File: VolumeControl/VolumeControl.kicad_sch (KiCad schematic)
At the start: 10 parts, among them J1 Barrel_Jack, U1 OPA1612AxD, U2 MCP4251-xxxx-SL, U3 L7812

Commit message: adv1
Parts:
- added C4: C, symbol Device:C
- added R2: R, symbol Device:R
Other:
- moved on the sheet: R1

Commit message: 6 Opamps
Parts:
- removed D1: 1N4001, Diode_THT:D_DO-41_SOD81_P10.16mm_Horizontal, symbol Diode:1N4001
- added C10, C11, C14, C15, C16, C17, C20, C21, C7, C8, C9: 10u, symbol Device:C
- added C12, C13, C18, C19, C5, C6: 50p, symbol Device:C
- added J10, J11, J12, J13, J2, J3, J4, J5, J6, J7, J8, J9: Conn_01x03, symbol Connector_Generic:Conn_01x03
- added R10, R11, R12, R3, R4, R5, R6, R7, R8, R9: 100k, Resistor_SMD:R_0805_2012Metric, symbol Device:R
- added U4, U6: MCP4251-xxxx-SL, Package_SO:SOIC-14_3.9x8.7mm_P1.27mm, symbol Potentiometer_Digital:MCP4251-xxxx-SL
- added U5, U7: OPA1612AxD, symbol Amplifier_Operational:OPA1612AxD
- C4: value C -> 10u
- R2: value R -> 100k; footprint (none) -> Resistor_SMD:R_0805_2012Metric
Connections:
- net GND: now also C1.2, C2.2, C3.2, J1.2, R1.2, R2.2, U1.4 (V-), U2.4 (VSS), C12.1, C13.1, C18.1, C19.1, C5.1, C6.1, J10.1 (Pin_1), J11.1 (Pin_1), J12.1 (Pin_1), J13.1 (Pin_1), J2.1 (Pin_1), J3.1 (Pin_1), J4.1 (Pin_1), J5.1 (Pin_1), J6.1 (Pin_1), J7.1 (Pin_1), J8.1 (Pin_1), J9.1 (Pin_1), R10.2, R11.2, R12.2, R3.2, R4.2, R5.2, R6.2, R7.2, R8.2, R9.2, U4.4 (VSS), U6.4 (VSS)
- net REF: now also U4.10 (P0B), U4.5 (P1B), U6.10 (P0B), U6.5 (P1B)
- net at R1.1: now also C4.2, J3.2 (Pin_2)
- net at C4.1: now also U1.1, U1.2 (-), C5.2
- net at U1.6 (-), U1.7: now also C6.2, C7.1
- net VCC: now reaches C1.1
- net VCC: now also C2.1, U1.8 (V+), U2.14 (VDD), U3.3 (OUT), U4.14 (VDD), U6.14 (VDD)
- net at R2.1: now also C7.2, J4.2 (Pin_2)
- net at C3.1: now also D2.1 (K), U3.1 (IN)
- net at U2.7 (P1A): now also C8.2
- net at U2.8 (P0A): now also C9.2
- net at D2.2 (A): now also J1.1
- new net: C18.2, C20.1, U7.1, U7.2 (-)
- new net: C20.2, J12.2 (Pin_2), R11.1
- new net: U4.6 (P1W), U5.5 (+)
- new net: C10.2, U4.7 (P1A)
- new net: C11.2, U4.8 (P0A)
- new net: U4.9 (P0W), U5.3 (+)
- new net: C9.1, J5.2 (Pin_2), R4.1
- new net: C19.2, C21.1, U7.6 (-), U7.7
- new net: C21.2, J13.2 (Pin_2), R12.1
- new net: C12.2, C14.1, U5.1, U5.2 (-)
- new net: C17.1, J11.2 (Pin_2), R10.1
- new net: C8.1, J2.2 (Pin_2), R3.1
- new net: C16.1, J10.2 (Pin_2), R9.1
- new net: U6.6 (P1W), U7.5 (+)
- new net: C16.2, U6.7 (P1A)
- new net: C17.2, U6.8 (P0A)
- new net: U6.9 (P0W), U7.3 (+)
- new net: C13.2, C15.1, U5.6 (-), U5.7
- new net: C15.2, J9.2 (Pin_2), R8.1
- new net: C10.1, J6.2 (Pin_2), R5.1
- new net: C14.2, J8.2 (Pin_2), R7.1
- new net: C11.1, J7.2 (Pin_2), R6.1
- new net Earth: J10.3 (Pin_3), J11.3 (Pin_3), J12.3 (Pin_3), J13.3 (Pin_3), J2.3 (Pin_3), J3.3 (Pin_3), J4.3 (Pin_3), J5.3 (Pin_3), J6.3 (Pin_3), J7.3 (Pin_3), J8.3 (Pin_3), J9.3 (Pin_3)
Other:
- moved on the sheet: C1, C2, C3, C4, D2, J1, R1, U1A, U1B, U1C, U2, U3

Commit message: circuito quase completo
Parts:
- added C22, C23: 50p, Capacitor_SMD:C_0805_2012Metric_Pad1.18x1.45mm_HandSolder, symbol Device:C
- added C24, C25, C26, C27, C28: 100nF, Capacitor_SMD:C_0805_2012Metric, symbol Device:C
- added C29: 100uF, Capacitor_SMD:CP_Elec_5x3.9, symbol Device:C_Polarized
- added R13, R14, R15: 100k, Resistor_SMD:R_0805_2012Metric, symbol Device:R
- added U10: LM1117MP-5.0, Package_TO_SOT_SMD:SOT-223-3_TabPin2, symbol Regulator_Linear:LM1117MP-5.0
- added U8: OPA1612AxD, Package_SO:SOIC-8-1EP_3.9x4.9mm_P1.27mm_EP2.29x3mm, symbol Amplifier_Operational:OPA1612AxD
- added U9: WEMOS_D1_mini, RF_Module:WEMOS_D1_mini_light, symbol RF_Module:WEMOS_D1_mini
- C1: footprint Capacitor_SMD:C_0805_2012Metric -> Capacitor_SMD:C_0805_2012Metric_Pad1.18x1.45mm_HandSolder
- C10, C11, C14, C15, C16, C17, C20, C21, C4, C7, C8, C9: footprint (none) -> Capacitor_SMD:C_1210_3225Metric_Pad1.33x2.70mm_HandSolder
- C12, C13, C18, C19, C5, C6: footprint (none) -> Capacitor_SMD:C_0805_2012Metric_Pad1.18x1.45mm_HandSolder
- C2, C3: value C_Polarized -> 100uF; footprint (none) -> Capacitor_SMD:CP_Elec_5x3.9
- J1: footprint (none) -> Connector_BarrelJack:BarrelJack_CUI_PJ-063AH_Horizontal
- J10, J11, J12, J13, J2, J3, J4, J5, J6, J7, J8, J9: footprint (none) -> Connector_PinHeader_1.00mm:PinHeader_1x03_P1.00mm_Vertical
- U1, U5, U7: footprint (none) -> Package_SO:SOIC-8-1EP_3.9x4.9mm_P1.27mm_EP2.29x3mm
- U3: footprint (none) -> Package_TO_SOT_SMD:TO-252-3_TabPin2
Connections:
- net GND: now also U5.4 (V-), U7.4 (V-), C22.1, C23.1, C24.2, C25.2, C26.2, C27.2, C28.2, C29.2, R13.2, R15.2, U10.1 (GND), U8.4 (V-), U9.10 (GND)
- net REF: now also C23.2, U8.1, U8.2 (-)
- net VCC: now also U5.8 (V+), U7.8 (V+), C24.1, C25.1, C26.1, C27.1, R14.1, U10.3 (VI), U8.8 (V+)
- new net: R15.1, U8.7
- new net: C22.2, R13.1, R14.2, U8.3 (+)
- new net V5V: C28.1, C29.1, U10.2 (VO), U9.9 (5V)
- no-connect marks 0 -> 2
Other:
- moved on the sheet: C1, C2, C3, D2, J1, U1C, U3

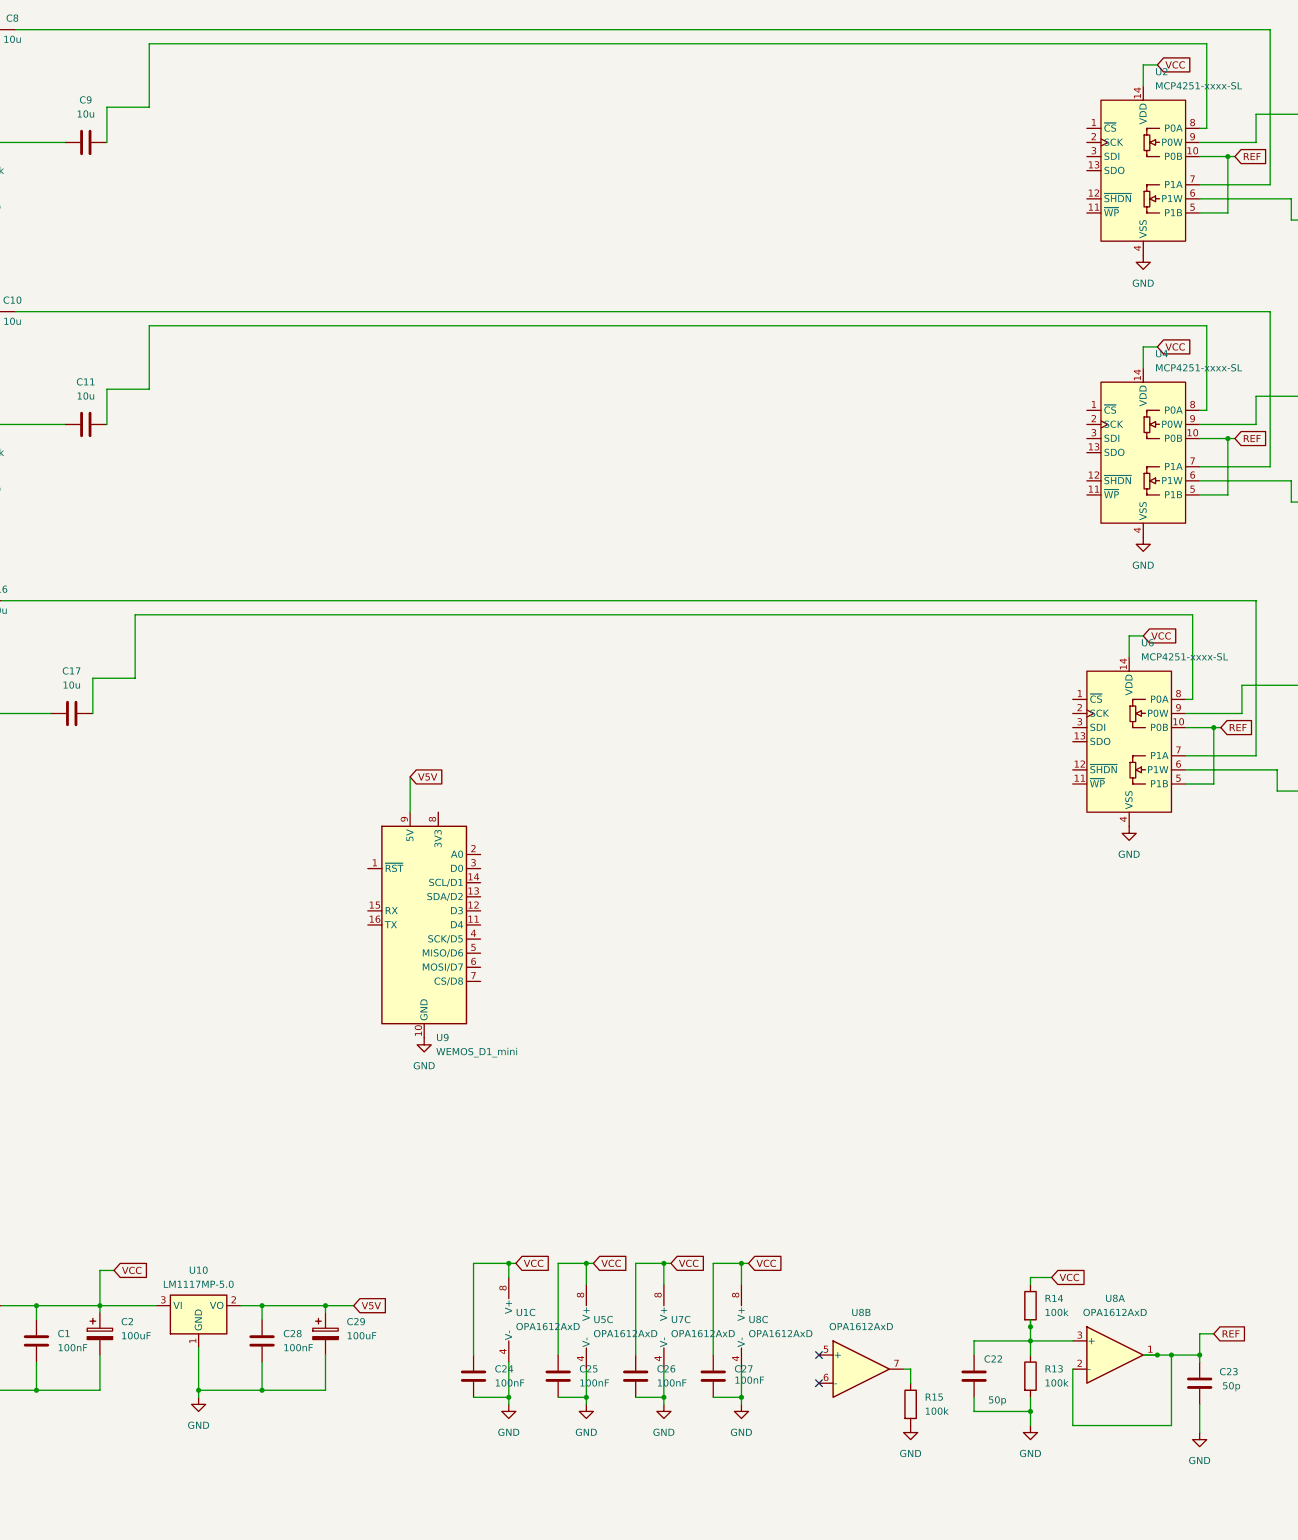
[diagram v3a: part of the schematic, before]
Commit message: changing power supply of dig potentiometers
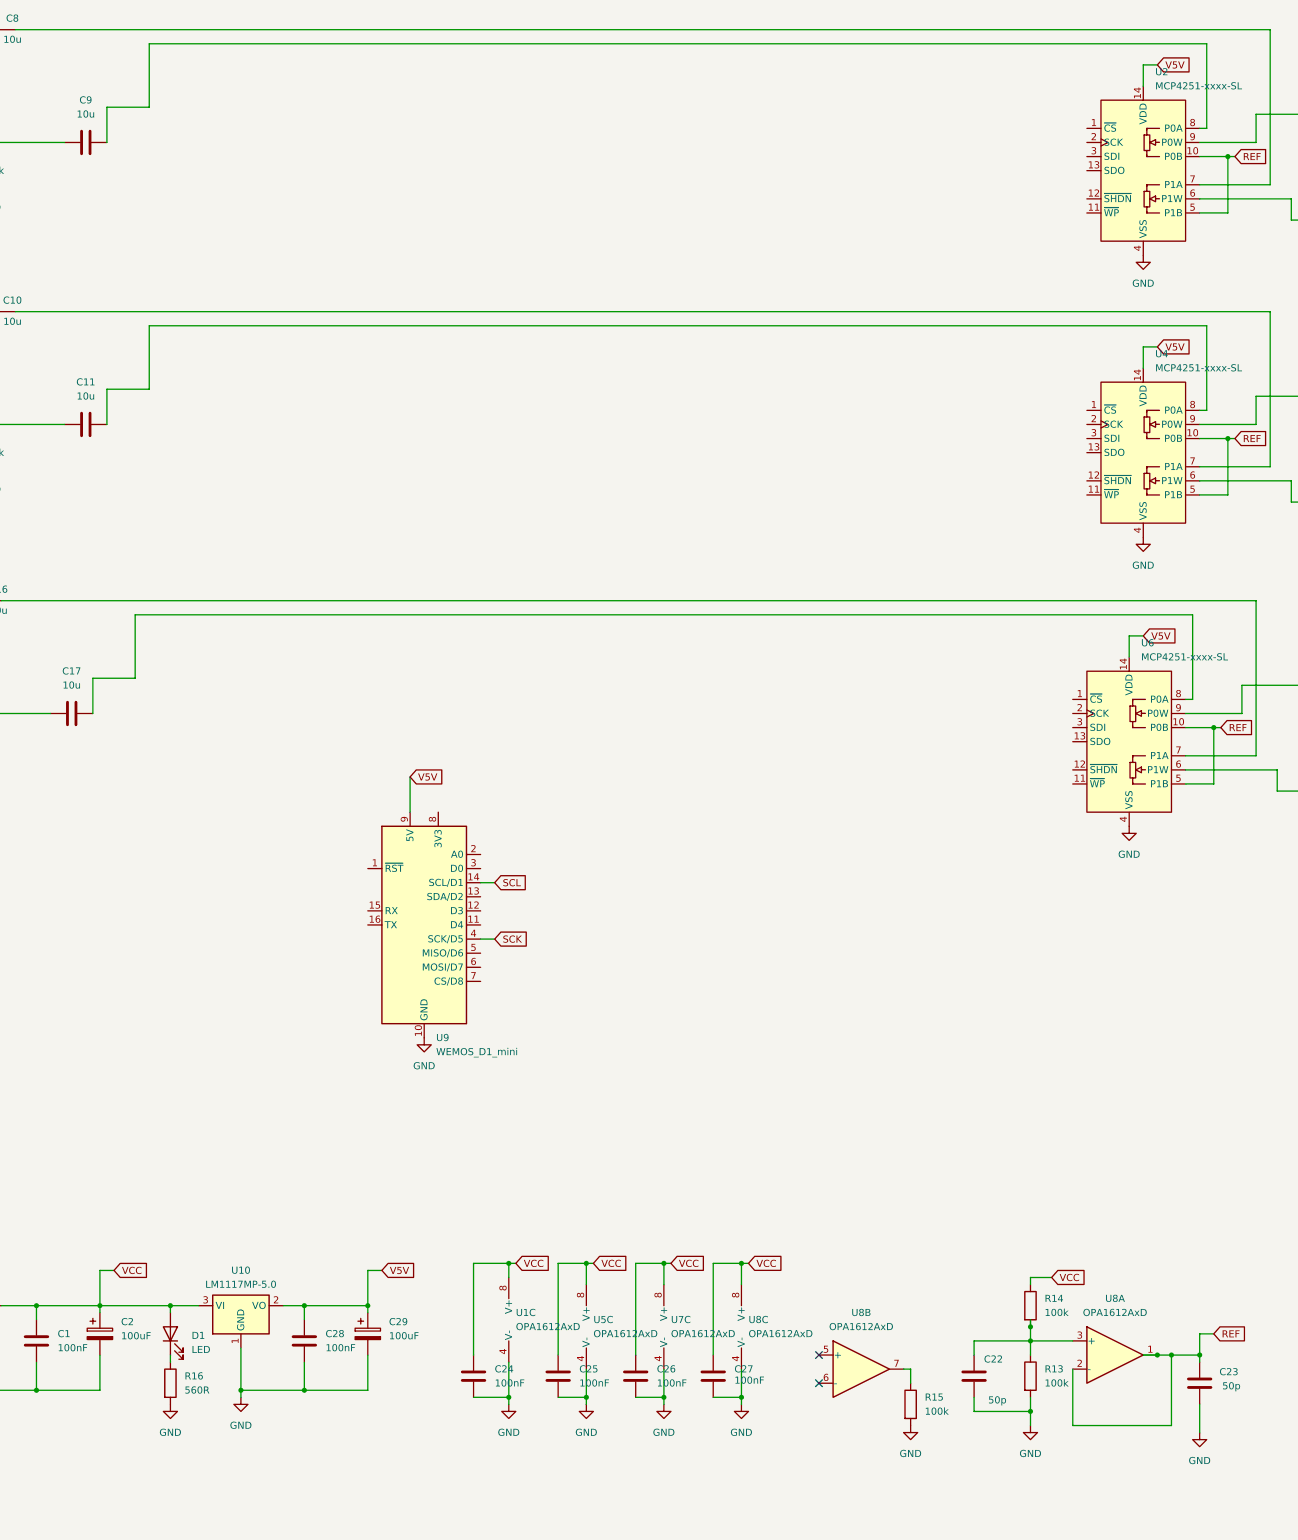
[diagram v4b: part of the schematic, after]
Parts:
- added D1: LED, symbol Device:LED
- added R16: 560R, Resistor_SMD:R_0805_2012Metric, symbol Device:R
- added unit 3 of U5
- added unit 3 of U7
- added unit 2 of U8
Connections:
- net GND: now also R16.2, U5.4 (V-), U7.4 (V-); no longer U5.4 (V-), U7.4 (V-)
- net V5V: now also U2.14 (VDD), U4.14 (VDD), U6.14 (VDD)
- net VCC: now also D1.2 (A), U5.8 (V+), U7.8 (V+); no longer U2.14 (VDD), U4.14 (VDD), U5.8 (V+), U6.14 (VDD), U7.8 (V+)
- net SCL: now reaches U9.14 (SCL/D1)
- net SCK: now reaches U9.4 (SCK/D5)
- net at R15.1: now also U8.7; no longer U8.7
- new net: D1.1 (K), R16.1
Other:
- moved on the sheet: C28, C29, U10

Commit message: layout upates
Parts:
- D1: footprint (none) -> LED_SMD:LED_1210_3225Metric
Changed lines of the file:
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@@
 			)
 		)
-		(property "Footprint" ""
+		(property "Footprint" "LED_SMD:LED_1210_3225Metric"
 			(at 104.14 255.27 0)
 			(effects

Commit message: improvements on PCB design - PCB placement finished -missing controller
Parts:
- added FB1: FerriteBead_Small, Resistor_SMD:R_1206_3216Metric_Pad1.30x1.75mm_HandSolder, symbol Device:FerriteBead_Small
- added R17: 10R, Resistor_SMD:R_0805_2012Metric, symbol Device:R
- U1, U5, U7, U8: footprint Package_SO:SOIC-8-1EP_3.9x4.9mm_P1.27mm_EP2.29x3mm -> Package_SO:SOIC-8_3.9x4.9mm_P1.27mm
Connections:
- net Earth: now also FB1.1, R17.1
- net GND: now also FB1.2, R17.2

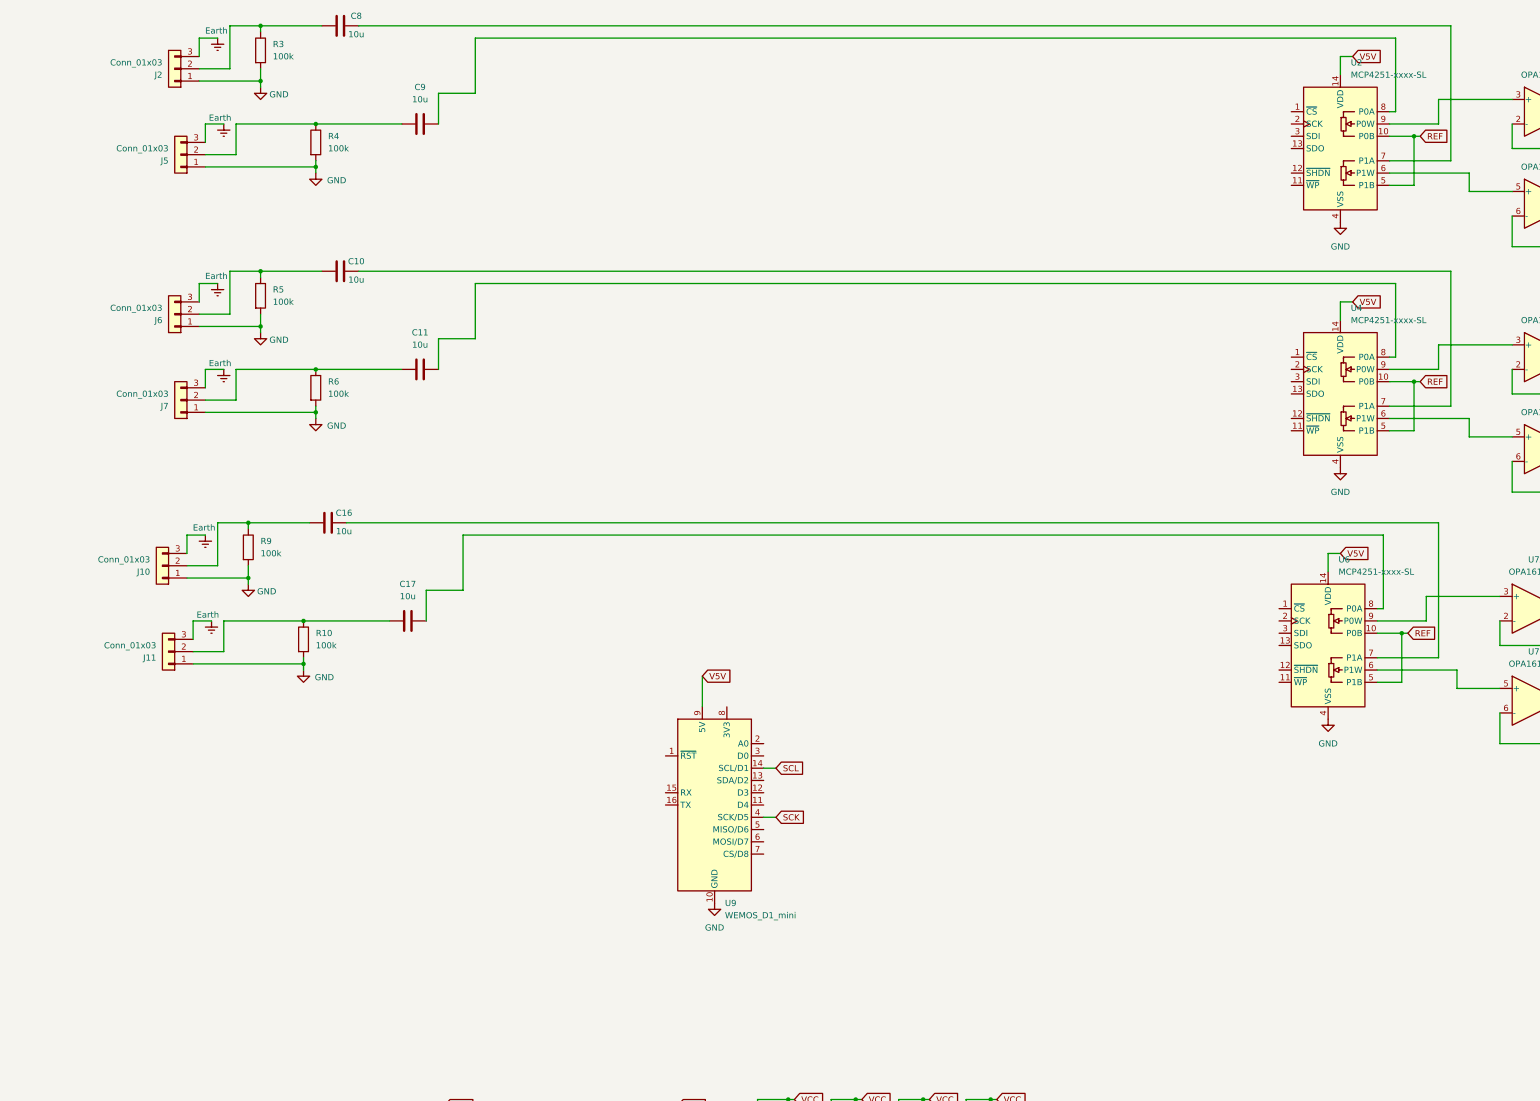
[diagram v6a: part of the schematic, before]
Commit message: simulation update, schematic update for only one input
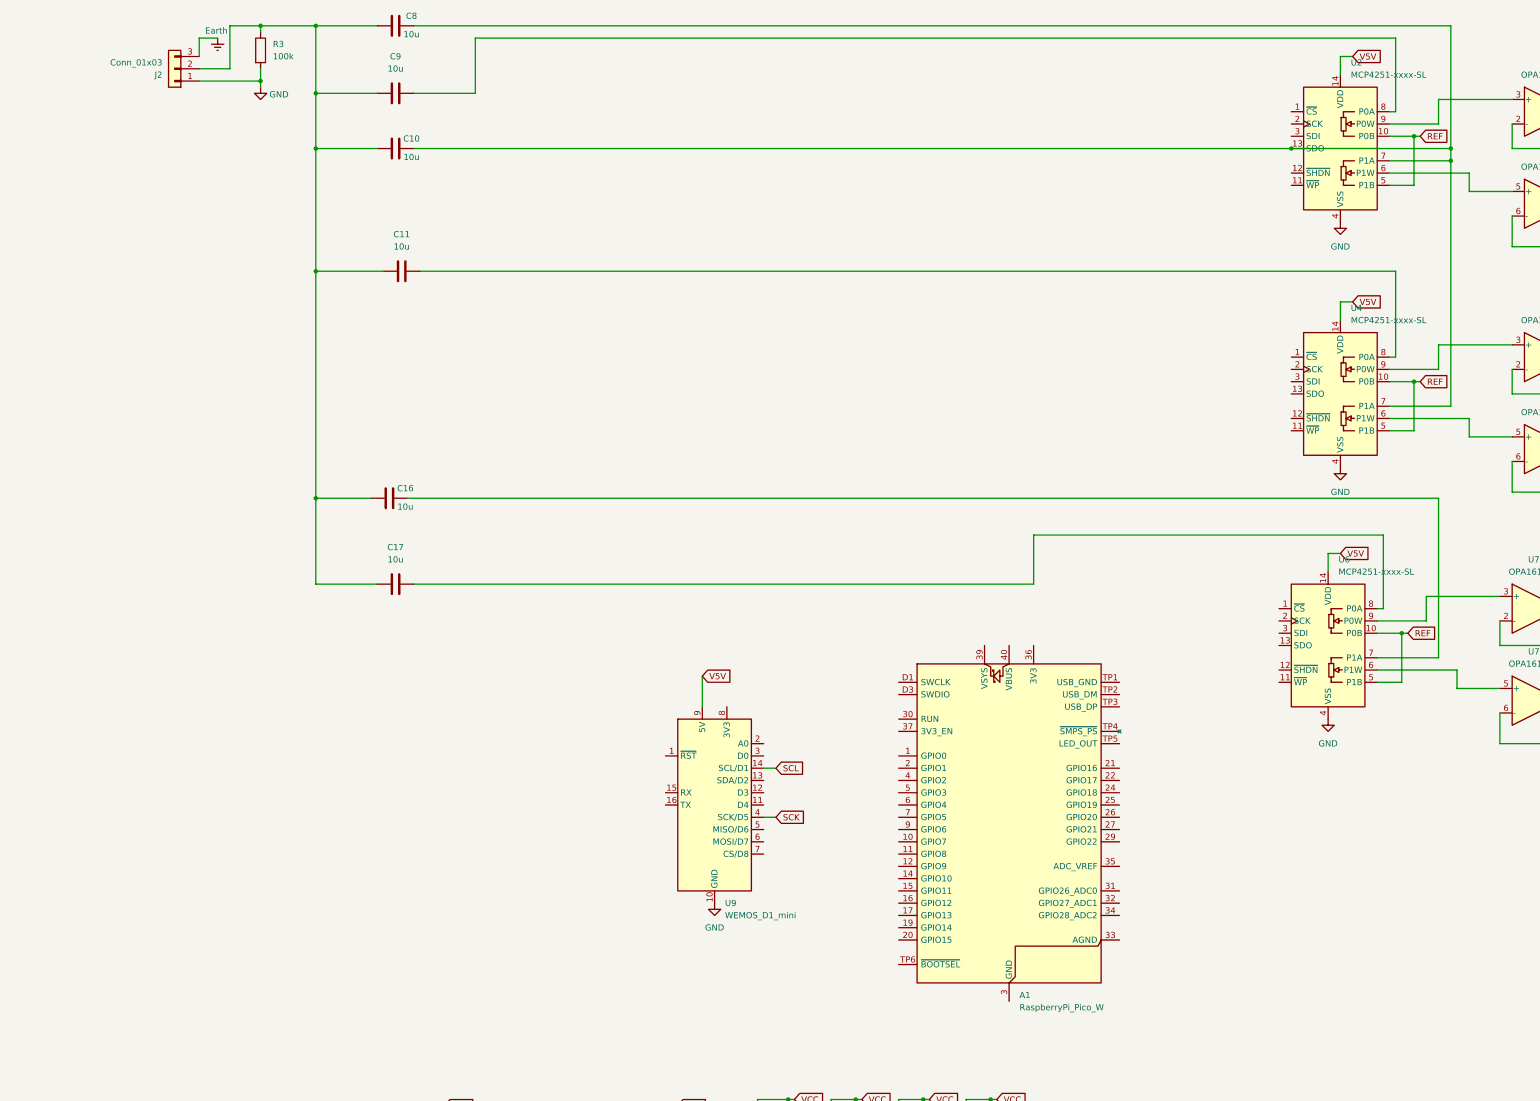
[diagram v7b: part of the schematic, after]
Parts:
- removed J10, J11, J5, J6, J7: Conn_01x03, Connector_PinHeader_1.00mm:PinHeader_1x03_P1.00mm_Vertical, symbol Connector_Generic:Conn_01x03
- removed R10, R4, R5, R6, R9: 100k, Resistor_SMD:R_0805_2012Metric, symbol Device:R
- added A1: RaspberryPi_Pico_W, Module:RaspberryPi_Pico_W_SMD, symbol MCU_Module:RaspberryPi_Pico_W_Extensive
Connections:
- net at C10.2, U4.7 (P1A): now also C8.2, U2.13 (SDO), U2.7 (P1A)
- net at C9.1: now also C10.1, C11.1, C16.1, C17.1, C8.1, J2.2 (Pin_2), R3.1
- new net: A1.13 (GND), A1.18 (GND), A1.23 (GND), A1.28 (GND), A1.3 (GND), A1.38 (GND), A1.8 (GND), A1.D2 (GND)
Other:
- moved on the sheet: C10, C11, C16, C17, C8, C9
